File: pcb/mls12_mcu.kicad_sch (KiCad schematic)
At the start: 35 parts, among them J2 TC2070-FP, J3 SM04B-SRSS-TB, U4 STM32H563RIT6, Y2 25MHz

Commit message: Route +3V3
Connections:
- net PHY_RST: now also U4.4 (PC15); no longer U4.20 (PA4)
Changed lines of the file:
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@@
-	(wire
-		(pts
-			(xy 109.22 195.58) (xy 109.22 194.31)
-		)
-		(stroke
-			(width 0)
-			(type default)
-		)
-	)
 	(wire
 		(pts
@@
 		)
 	)
-	(wire
-		(pts
-			(xy 109.22 194.31) (xy 116.84 194.31)
-		)
-		(stroke
-			(width 0)
-			(type default)
-		)
-	)
 	(bus
 		(pts
@@
 	(wire
 		(pts
-			(xy 86.36 195.58) (xy 109.22 195.58)
-		)
-		(stroke
-			(width 0)
-			(type default)
-		)
-	)
-	(wire
-		(pts
 			(xy 113.03 81.28) (xy 113.03 82.55)
 		)
@@
 		(pts
 			(xy 88.9 190.5) (xy 113.03 190.5)
+		)
+		(stroke
+			(width 0)
+			(type default)
+		)
+	)
+	(wire
+		(pts
+			(xy 237.49 222.25) (xy 260.35 222.25)
 		)
 		(stroke
@@
 	(hierarchical_label "PHY_RST"
 		(shape output)
-		(at 116.84 194.31 0)
-		(effects
-			(font
+		(at 260.35 222.25 0)
+		(effects
+			(font

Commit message: Route PHY IRQ
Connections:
- net ~{PHY_IRQ}: now reaches U4.17 (PA3)
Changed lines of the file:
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@@
 	(wire
 		(pts
+			(xy 86.36 193.04) (xy 116.84 193.04)
+		)
+		(stroke
+			(width 0)
+			(type default)
+		)
+	)
+	(wire
+		(pts
 			(xy 72.39 73.66) (xy 72.39 58.42)
 		)
@@
 		)
 	)
+	(hierarchical_label "~{PHY_IRQ}"
+		(shape input)
+		(at 116.84 193.04 0)
+		(effects
+			(font
+				(size 1.27 1.27)
+			)
+			(justify left)
+		)
+	)
 	(hierarchical_label "PHY{RMII}"
 		(shape bidirectional)
@@
 		)
 		(pin "17"
-			(alternate "PA3_ADC1_INP15")
 		)
 		(instances

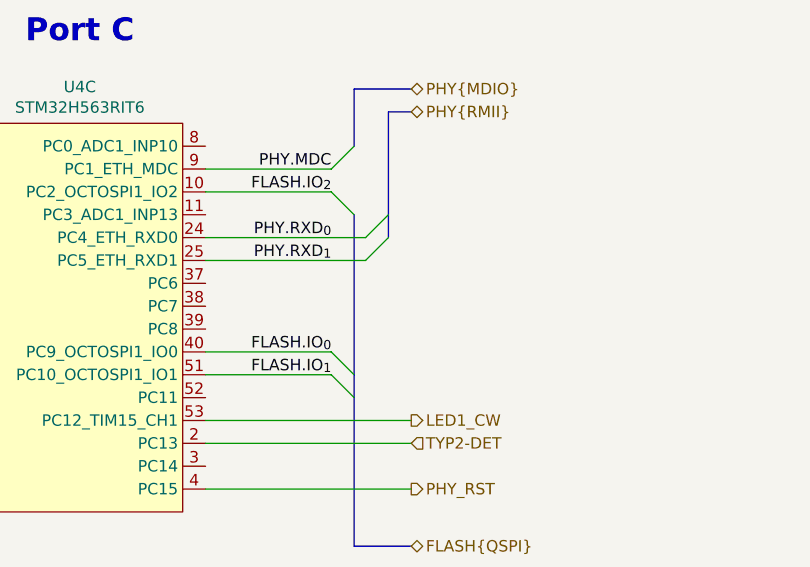
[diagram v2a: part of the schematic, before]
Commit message: Add blinky LED
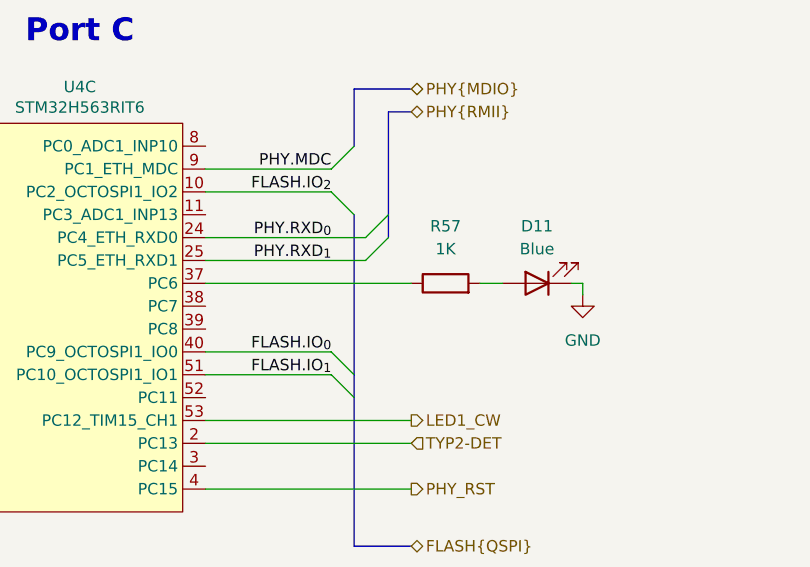
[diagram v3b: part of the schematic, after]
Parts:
- added D11: Blue, LED_SMD:LED_0603_1608Metric, symbol Device:LED
- added R57: 1K, Resistor_SMD:R_0603_1608Metric, symbol Device:R
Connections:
- net GND: now also D11.1 (K)
- net at U4.37 (PC6): now also R57.1
- new net: D11.2 (A), R57.2

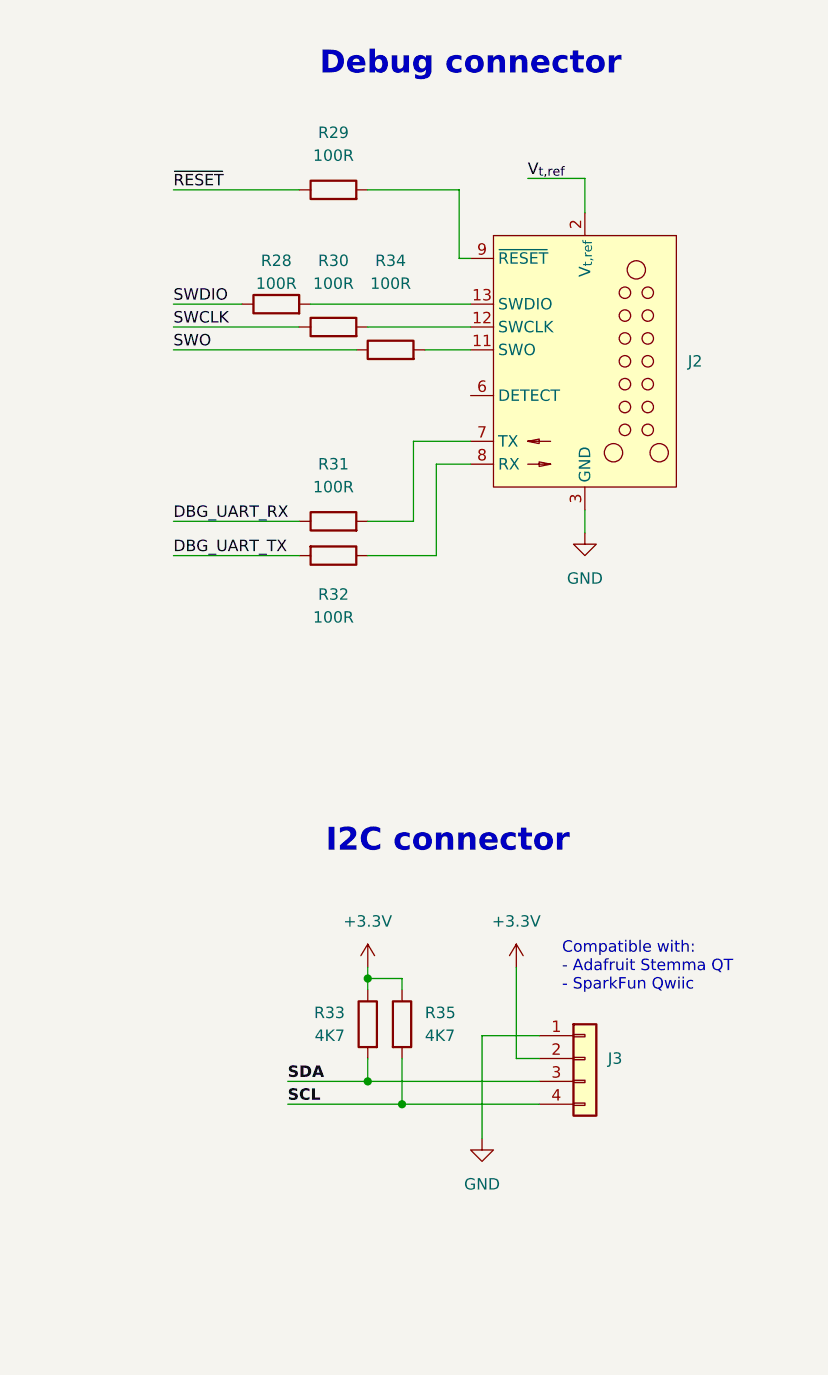
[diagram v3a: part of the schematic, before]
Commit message: Add test points
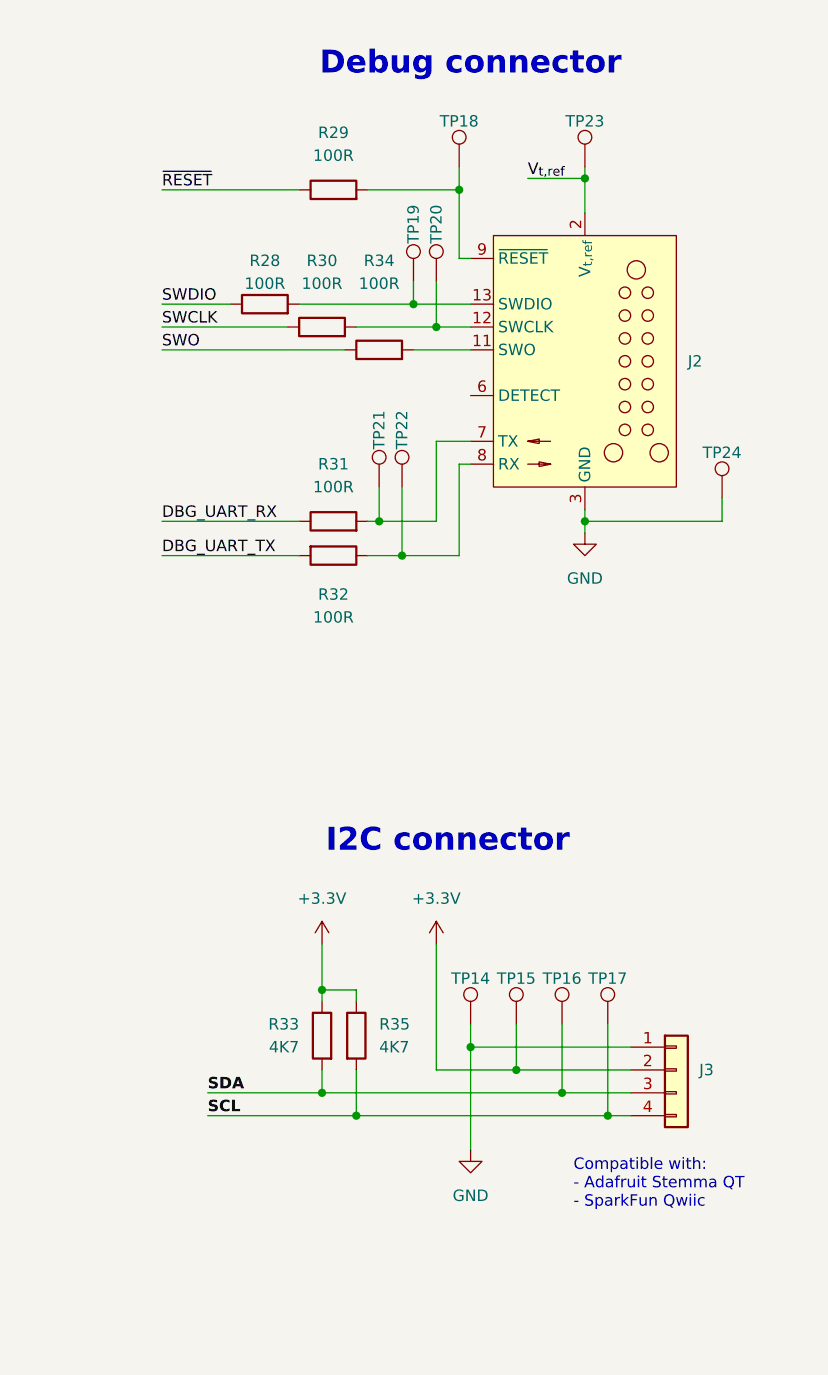
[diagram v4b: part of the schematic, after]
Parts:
- added TP14, TP24: TestPoint, TestPoint:TestPoint_Pad_1.5x1.5mm, symbol Connector:TestPoint
- added TP15, TP16, TP17, TP18, TP19, TP20, TP21, TP22, TP23: TestPoint, TestPoint:TestPoint_Pad_D1.5mm, symbol Connector:TestPoint
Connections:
- net +3.3V: now also TP15.1
- net GND: now also TP14.1, TP24.1
- net SCL: now also TP17.1
- net SDA: now also TP16.1
- net V_{t,ref}: now also TP23.1
- net at J2.12 (SWCLK), R30.2: now also TP20.1
- net at J2.13 (SWDIO), R28.2: now also TP19.1
- net at J2.7 (TX), R31.2: now also TP21.1
- net at J2.8 (RX), R32.1: now also TP22.1
- net at J2.9 (~{RESET}), R29.2: now also TP18.1
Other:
- moved on the sheet: J3, R28, R30, R33, R34, R35
